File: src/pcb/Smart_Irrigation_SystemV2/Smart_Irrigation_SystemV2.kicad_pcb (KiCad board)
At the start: 4 copper layers, 100 x 55.5 mm, 130 parts, among them CN1 PJ-3136-3A, CN2 PJ-3136-3A, CN3 PJ-3136-3A, CN4 PJ-3136-3A, CN5 PJ-3136-3A, CN6 PJ-3136-3A, J1 USB_C_Receptacle_USB2.0_16P, J10 I2C, J11 I2C, J13 I2C, J14 SolarPanel, J15 I2C, J16 GPIO_Expander, J2 FPC_Connector, J6 I2C, J9 Battary Connection, Q1 MUN5211DW1, Q2 FDN340P, Q3 AO3400A, SW1 IO0 Switch, SW2 EN Switch, SW3 SW_Push, SW4 SW_Push, SW5 SW_Push, SW6 SW_Push, U1 CP2102N-Axx-xQFN28, U10 ADS1115IDGS, U11 PCA9536DP, U2 ESP32-WROOM-32, U3 ADS1115IDGS, U4 DS3231MZ, U5 TLV62568ADRL, U6 SN74LVC245APW, U7 TP4056-42-ESOP8, U8 TPS63001, U9 AT24CS32-SSHM

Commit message: added 3D models to the parts and modified shape of pcb
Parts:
- removed H1, H2, H3, H4: MountingHole_Pad, MountingHole:MountingHole_3.2mm_M3_DIN965_Pad
- CN1, CN2, CN3, CN4, CN5, CN6: footprint Test:AUDIO-TH_PJ-3136-3A -> C707248:AUDIO-TH_PJ-3136-3A
- J1: footprint Connector_USB:USB_C_Receptacle_HRO_TYPE-C-31-M-12 -> C5337088:USB-C-SMD_TYPE-C-31-M-12A
- L1: footprint Inductor_SMD:L_7.3x7.3_H3.5 -> C726315:IND-SMD_L7.1-W6.6
- L2: footprint Inductor_SMD:L_7.3x7.3_H3.5 -> C128686:IND-SMD_L6.6-W6.6
- MICRO_SD1: footprint TF-01A:TF-01A -> C91145:TF-SMD_TF-01A
- SW1, SW2: footprint Test:KEY-SMD_4P-L6.0-W6.0-P3.90-LS9.0 -> C83206:KEY-SMD_4P-L6.0-W6.0-P3.90-LS9.0
- U7: footprint Package_SO:SOIC-8-1EP_3.9x4.9mm_P1.27mm_EP2.41x3.3mm_ThermalVias -> C16581:ESOP-8_L4.9-W3.9-P1.27-LS6.0-BL-EP
- U8: footprint Package_SON:Texas_DRC0010J_ThermalVias -> C28060:VSON-10_L3.0-W3.0-P0.50-TL-EP_TPS62410DRCR
- moved MICRO_SD1 1.93 mm to (215.1, 106.8)
- moved J1 1.35 mm to (235.1, 124.2)
- turned U7 to -90 degrees
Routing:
- net GND: track 0.00 -> 138.3 mm, vias 0 -> 68
- net +5V: track 32.9 -> 109.6 mm, vias 0 -> 9
- net +3.3V: track 14.2 -> 74.8 mm, vias 0 -> 45
- net /VoltageBat: track 3.96 -> 56.3 mm, vias 0 -> 2
- net /GPIO27: track 31.8 -> 66.6 mm, vias 2 -> 4
- net /GPIO14: track 31.7 -> 47.2 mm, vias 2 -> 4
- net /VBUS_IN: track 22.3 -> 34.2 mm, vias 0 -> 2
- net /SCK: track 45.0 -> 47.1 mm, vias 0 -> 1
- net Net-(D5-K): track 0.00 -> 1.92 mm
- net /TXD: track 59.4 -> 57.5 mm
- net /EN: track 95.6 -> 93.7 mm
- net /CS: track 45.2 -> 46.5 mm
- net /SCL: track 199.8 -> 200.7 mm
- net /GPIO17: track 25.4 -> 26.0 mm
- added copper zone on In2.Cu, net +3.3V
- added copper zone on In1.Cu, net GND
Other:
- board size 100 x 55.5 mm -> 100 x 55.7 mm

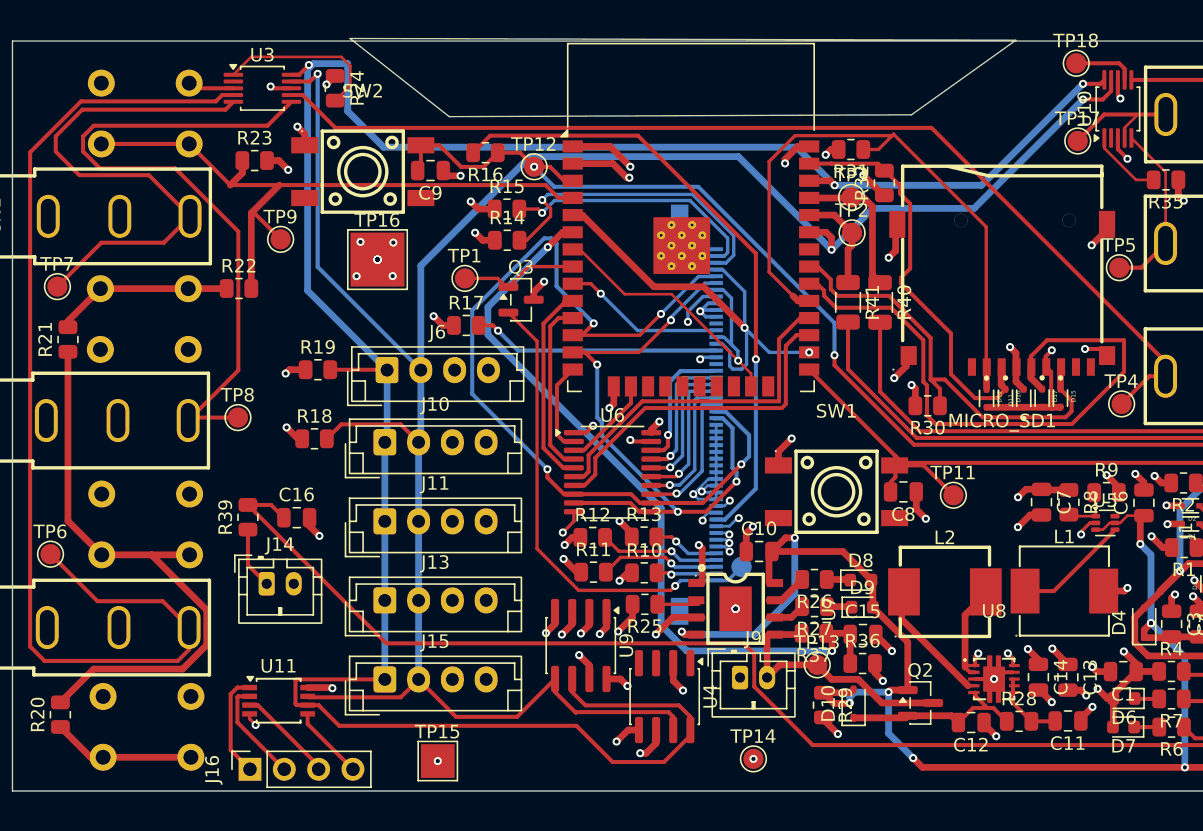
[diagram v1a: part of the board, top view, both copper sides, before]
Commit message: added decoupling capacitors
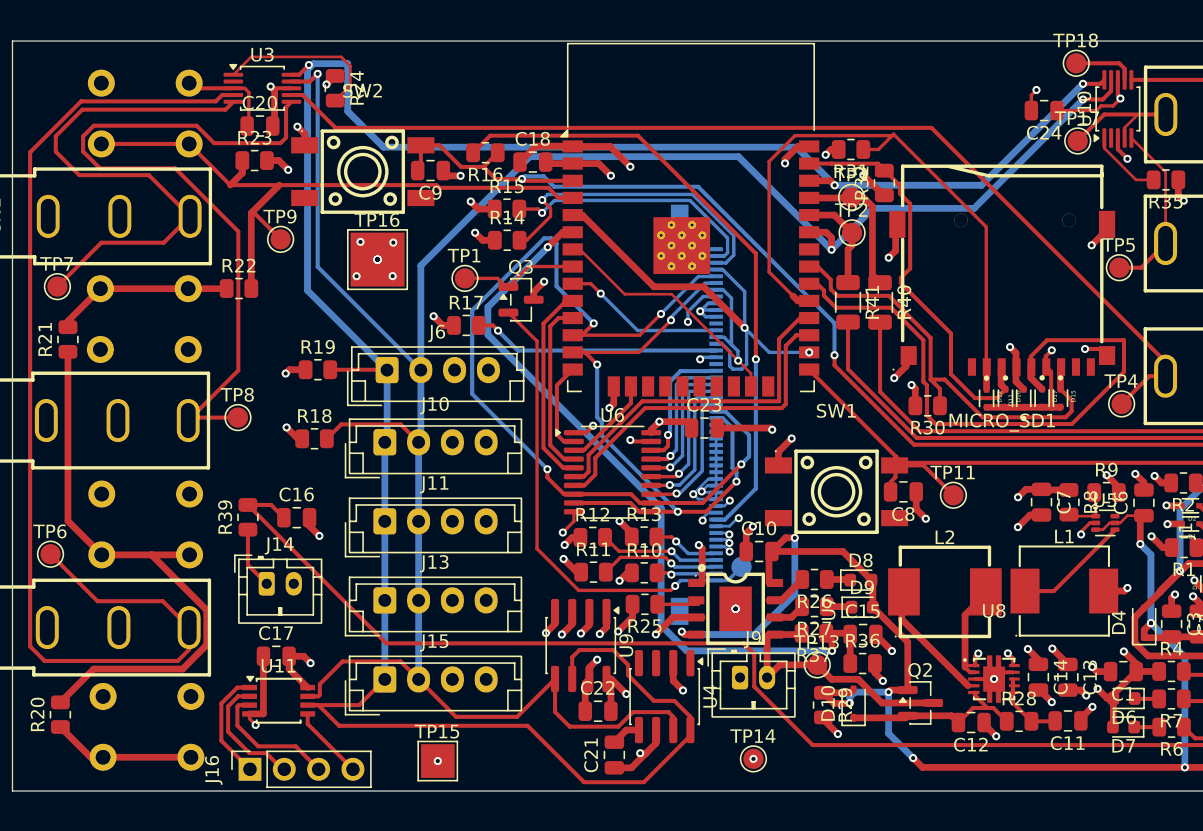
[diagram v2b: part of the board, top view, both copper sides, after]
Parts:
- removed TP12: EN, TestPoint:TestPoint_Pad_D1.5mm
- added C17: 100nF, Capacitor_SMD:C_0805_2012Metric, F.Cu at (161.4, 133.5)
- added C18: 100nF, Capacitor_SMD:C_0805_2012Metric, F.Cu at (180.4, 96.9)
- added C20: 100nF, Capacitor_SMD:C_0805_2012Metric, F.Cu at (160.2, 94.2)
- added C21: 100nF, Capacitor_SMD:C_0805_2012Metric, F.Cu at (186.4, 140.8)
- added C22: 100nF, Capacitor_SMD:C_0805_2012Metric, F.Cu at (185.2, 137.5)
- added C23: 100nF, Capacitor_SMD:C_0805_2012Metric, F.Cu at (193.1, 116.6)
- added C24: 100nF, Capacitor_SMD:C_0805_2012Metric, F.Cu at (218.2, 93.1)
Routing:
- net GND: track 138.3 -> 160.0 mm, vias 68 -> 69
- net +3.3V: track 74.8 -> 94.8 mm
- net /SDA: track 164.1 -> 167.3 mm
- net Net-(J16-Pin_3): track 7.22 -> 9.70 mm
- net /MS3: track 50.8 -> 53.2 mm
- net Net-(J16-Pin_2): track 7.71 -> 9.08 mm
- net /EN: track 93.7 -> 95.0 mm
- net /SCL: track 200.7 -> 201.7 mm
- net Net-(J16-Pin_1): track 7.75 -> 8.32 mm
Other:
- board size 100 x 55.7 mm -> 100 x 55.5 mm

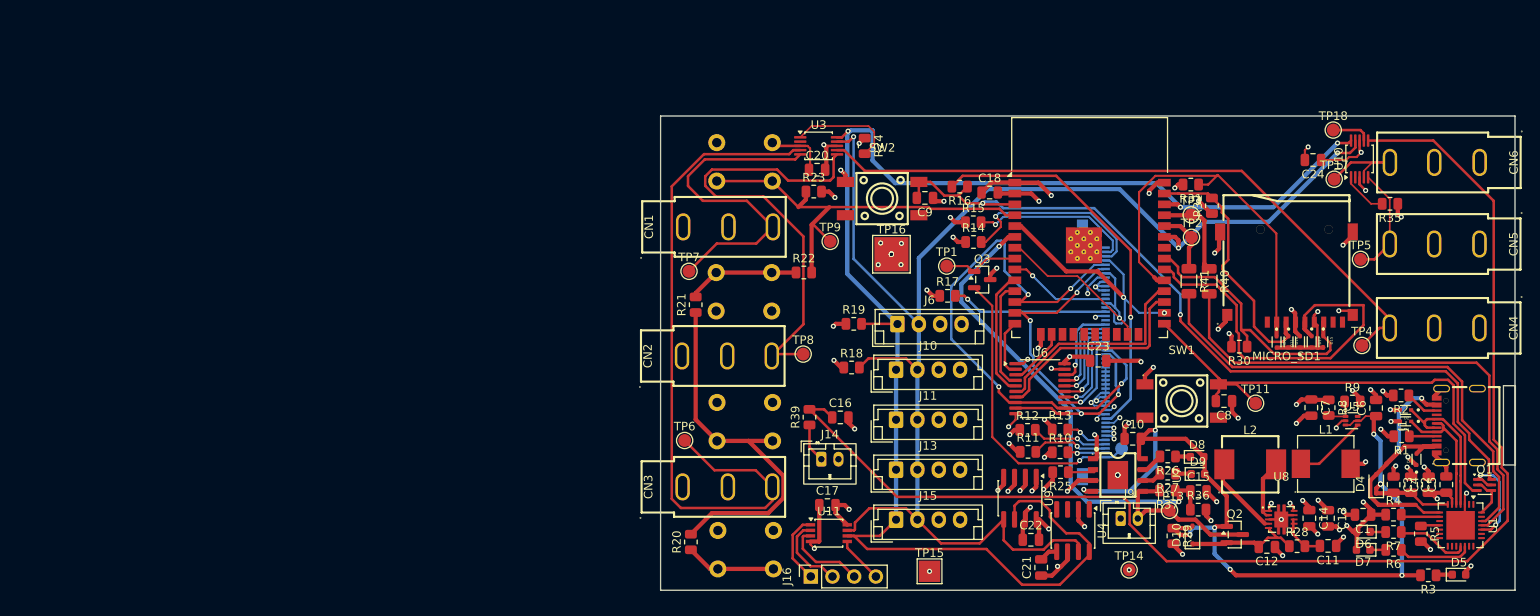
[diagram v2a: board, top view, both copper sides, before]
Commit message: changed pcb color, fixed design misakes (DRC), made new edge cuts, exported new image of the pcb
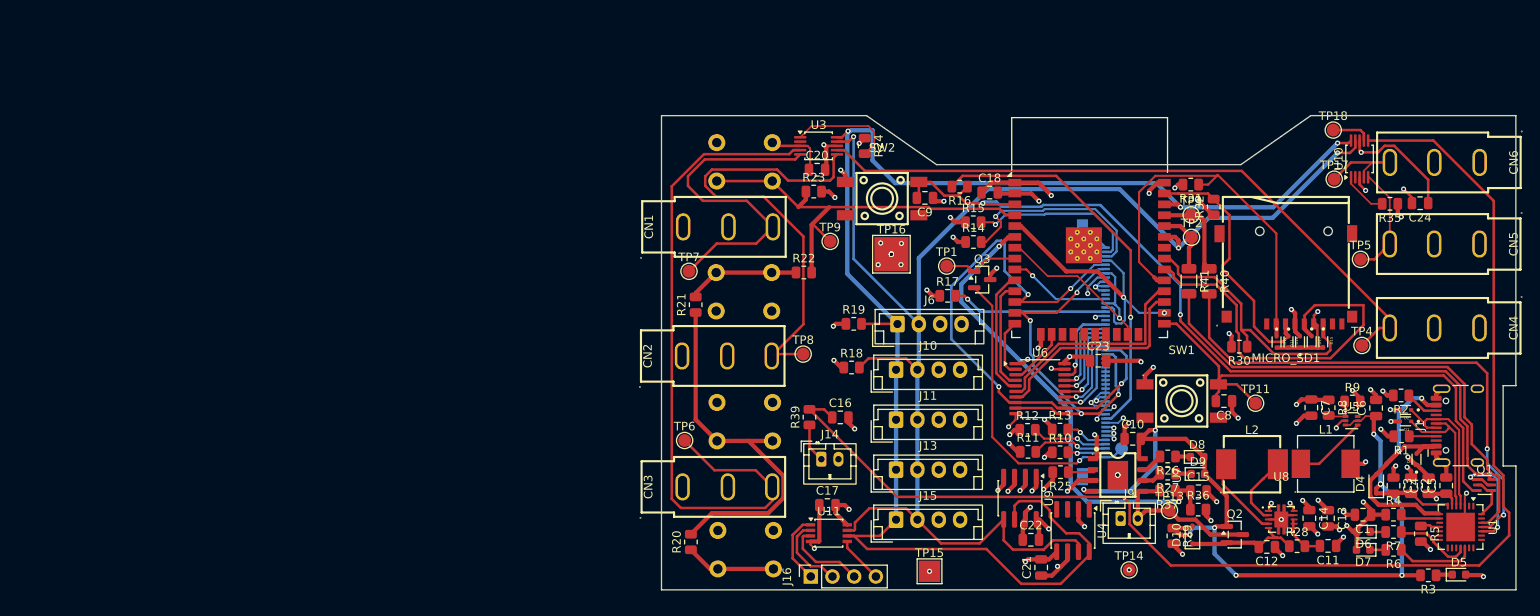
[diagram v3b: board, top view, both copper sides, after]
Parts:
- J1: footprint C5337088:USB-C-SMD_TYPE-C-31-M-12A -> Connector_USB:USB_C_Receptacle_HCTL_HC-TYPE-C-16P-01A
- moved C24 13.5 mm to (230.8, 98.2)
- moved J1 1.30 mm to (236.4, 124.2)
- moved R32 0.25 mm to (206.6, 98.6)
- moved MICRO_SD1 0.22 mm to (215.1, 107.0)
- moved L2 0.21 mm to (211.1, 128.7)
- moved U1 0.20 mm to (235.5, 136.0)
- moved C3 0.12 mm to (227.7, 131.2)
- moved C2 0.12 mm to (229.7, 131.2)
- moved C4 0.12 mm to (231.8, 131.2)
- moved C5 0.12 mm to (233.8, 131.2)
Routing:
- net +3.3V: track 94.8 -> 102.5 mm
- net /SCK: track 47.1 -> 45.0 mm, vias 1 -> 0
- net /RTS: track 12.3 -> 14.0 mm
- net /SolarPanel: track 151.2 -> 152.9 mm
- net /EN: track 95.0 -> 96.5 mm
- net Net-(U8-L2): track 7.19 -> 8.45 mm
- net GND: track 160.0 -> 158.9 mm, vias 69 -> 66
- net Net-(J2-Pin_48): track 23.3 -> 24.3 mm
- net Net-(J2-Pin_49): track 19.3 -> 20.2 mm
- net /GPIO0: track 58.3 -> 59.1 mm
- net Net-(U8-L1): track 9.51 -> 10.3 mm
- net /D-: track 15.7 -> 16.4 mm
- net Net-(U1-~{TXT}/GPIO.0): track 8.70 -> 9.39 mm
- net Net-(U1-~{RXT}/GPIO.1): track 8.54 -> 9.17 mm
- net /TXD: track 57.5 -> 58.1 mm
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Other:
- outline, holes or cut-outs redrawn

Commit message: improved routing
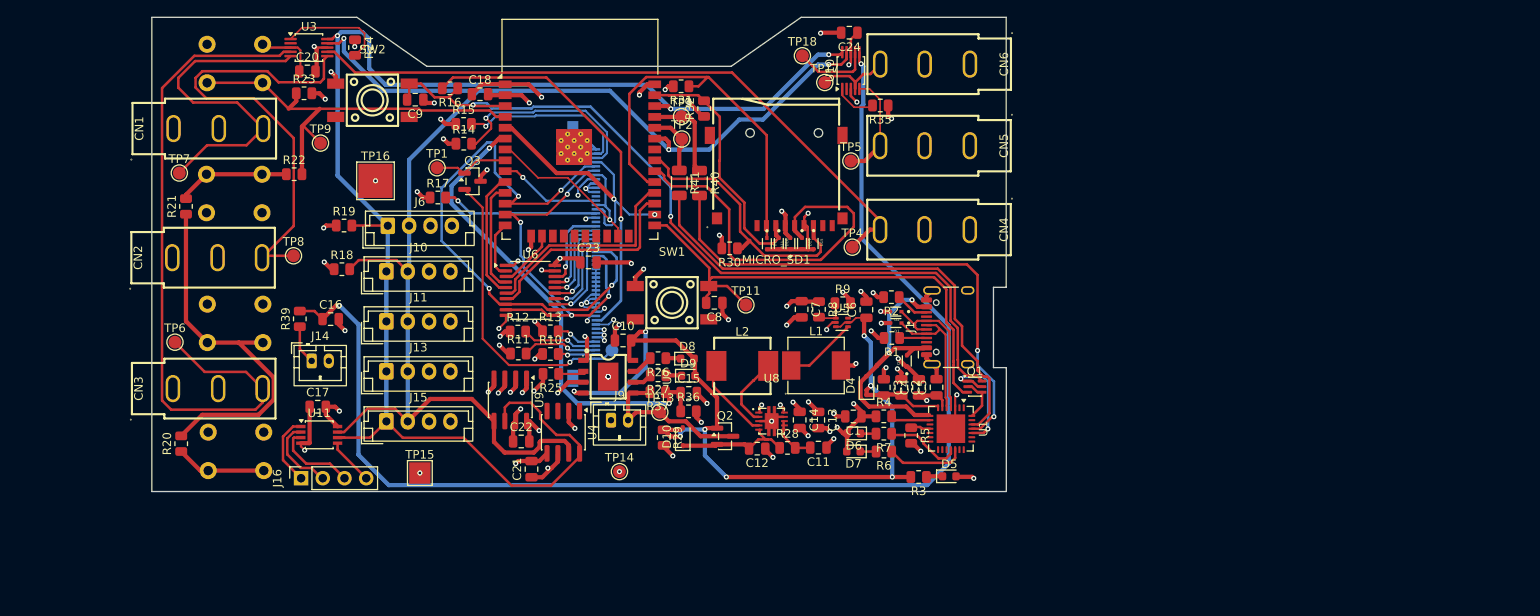
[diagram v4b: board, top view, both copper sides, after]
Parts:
- moved C24 69.7 mm to (164.0, 78.2)
- moved TP18 62.7 mm to (158.5, 80.9)
- moved TP16 61.0 mm to (108.5, 95.5)
- moved C10 60.7 mm to (137.5, 114.2)
- moved C12 60.7 mm to (153.2, 126.9)
- moved C13 60.7 mm to (160.3, 123.5)
- moved C14 60.7 mm to (158.2, 123.5)
- moved C15 60.7 mm to (145.2, 120.4)
- moved C16 60.7 mm to (103.3, 111.7)
- moved C17 60.7 mm to (101.8, 122.0)
- moved C18 60.7 mm to (120.8, 85.4)
- moved C2 60.7 mm to (170.1, 119.7)
- moved C21 60.7 mm to (126.8, 129.3)
- moved C22 60.7 mm to (125.6, 126.0)
- moved C23 60.7 mm to (133.5, 105.1)
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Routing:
- net +3.3V: track 102.5 -> 92.6 mm, vias 45 -> 35
- net /SDA: track 167.3 -> 161.1 mm
- net /SCL: track 201.6 -> 196.5 mm
- net /SolarPanel: track 152.9 -> 148.3 mm, vias 0 -> 2
- net Net-(U10-AIN3): track 4.57 -> 9.09 mm
- net /MS6: track 11.5 -> 9.55 mm
- net /MOSI: track 30.5 -> 29.8 mm
- net /MS5: track 13.1 -> 12.5 mm

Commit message: solved warnings from drc and menaged silkscreen
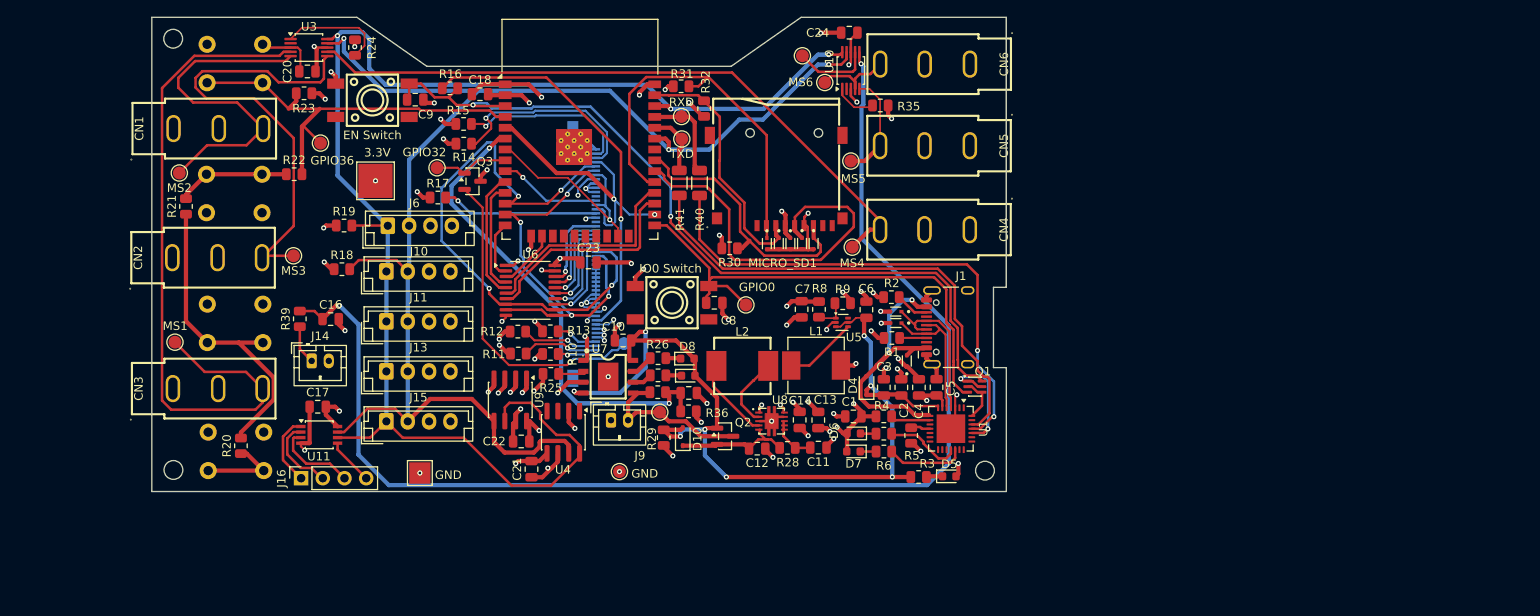
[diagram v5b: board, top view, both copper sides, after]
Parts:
- added H1: MountingHole, MountingHole:MountingHole_2.2mm_M2, F.Cu at (84.8, 78.9)
- added H2: MountingHole, MountingHole:MountingHole_2.2mm_M2, F.Cu at (84.9, 129.4)
- added H3: MountingHole, MountingHole:MountingHole_2.2mm_M2, F.Cu at (179.9, 129.4)
- moved R20 6.99 mm to (92.8, 126.5)
- moved TP10 1.61 mm to (137.6, 114.6)
- turned D11 to -90 degrees
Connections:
- D11 pad 1: GND -> +3.3V
- D11 pad 2: +3.3V -> GND
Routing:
- net Net-(R20-Pad2): track 43.5 -> 37.0 mm
- net Net-(J2-Pin_1): track 35.5 -> 37.2 mm
- net GND: track 159.2 -> 157.7 mm, vias 66 -> 63
- net /SCL: track 196.5 -> 195.7 mm
- net Net-(R20-Pad1): track 10.6 -> 10.00 mm
- net Net-(J9-Pin_2): track 19.5 -> 19.0 mm
- net +5V: vias 9 -> 8

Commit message: first gerber files, last polish
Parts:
- U8: footprint C28060:VSON-10_L3.0-W3.0-P0.50-TL-EP_TPS62410DRCR -> Package_TO_SOT_SMD:SOT-23-5
- moved U8 0.06 mm to (154.9, 123.6), turned to 180 degrees
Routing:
- net Net-(U8-EN): track 5.46 -> 1.77 mm
- net +5V: track 109.6 -> 111.1 mm, vias 8 -> 7
- net GND: track 157.7 -> 156.2 mm
- net Net-(U8-L2): track 8.45 -> 7.43 mm
- net Net-(U8-L1): track 10.3 -> 9.48 mm
- net +3.3V: track 93.0 -> 92.3 mm, vias 35 -> 34
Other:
- board text added: "Smart Irrigation System V2.0"
- board text added: "benedikt314159"
- board text added: "made by humans on earth without AI"

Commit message: production ready!
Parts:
- removed C17: 100nF, Capacitor_SMD:C_0805_2012Metric
- removed U9: AT24CS32-SSHM, Package_SO:SOIC-8_3.9x4.9mm_P1.27mm
- R20, R21, R22: moved to B.Cu
- SW3, SW4, SW5, SW6: footprint Button_Switch_THT:SW_PUSH_6mm_H4.3mm -> C83206:KEY-SMD_4P-L6.0-W6.0-P3.90-LS9.0
- U5: footprint Package_TO_SOT_SMD:SOT-563 -> Package_TO_SOT_SMD:SOT-23-5
- U8: footprint Package_TO_SOT_SMD:SOT-23-5 -> Package_SON:VSON-10-1EP_3x3mm_P0.5mm_EP1.65x2.4mm_ThermalVias
- moved C22 24.1 mm to (101.8, 122.2)
- moved R21 17.6 mm to (100.0, 109.6)
- moved R20 7.54 mm to (99.9, 124.2)
- moved SW6 5.18 mm to (93.0, 81.0)
- moved SW3 4.64 mm to (93.0, 127.2), turned to 180 degrees
- moved SW4 4.62 mm to (93.0, 112.4), turned to 180 degrees
- moved TP9 3.24 mm to (100.6, 88.2)
- moved SW5 3.07 mm to (93.0, 96.9)
- moved R22 1.45 mm to (100.3, 94.0), turned to 90 degrees
- moved C21 1.30 mm to (126.8, 128.0)
- moved C7 1.14 mm to (157.3, 110.3)
- moved R8 1.14 mm to (159.3, 110.3)
- moved R9 0.84 mm to (162.7, 109.2)
- moved U8 0.50 mm to (154.6, 123.2), turned to 0 degrees
- moved U5 0.43 mm to (162.7, 111.9)
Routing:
- net Net-(R20-Pad2): track 37.0 -> 15.5 mm
- net GND: track 156.2 -> 171.5 mm, vias 63 -> 59
- net /SCL: track 195.7 -> 181.2 mm
- net Net-(R20-Pad1): track 10.00 -> 2.69 mm
- net +3.3V: track 92.3 -> 87.9 mm
- net Net-(U8-EN): track 1.77 -> 6.03 mm
- net /GPIO36: track 50.2 -> 46.3 mm, vias 0 -> 1
- net Net-(R21-Pad2): track 13.2 -> 16.8 mm
- net /SDA: track 161.1 -> 158.2 mm
- net +5V: track 111.1 -> 113.2 mm
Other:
- board text added: "Smart Irrigation System V2.2"
- board text removed: "Smart Irrigation System V2.0"
